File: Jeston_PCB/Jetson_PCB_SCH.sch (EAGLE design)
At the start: 4 parts, among them Q2 NTD3055L104G

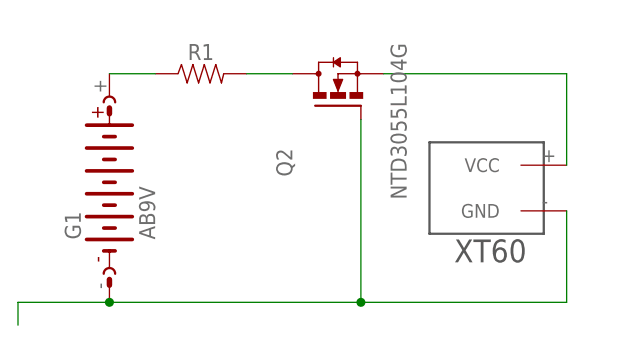
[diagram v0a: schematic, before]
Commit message: replaced battery port with XT60
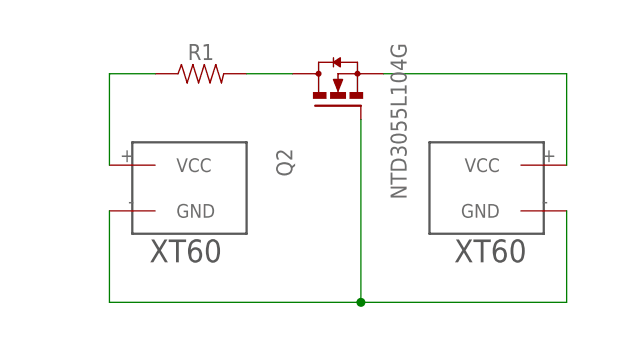
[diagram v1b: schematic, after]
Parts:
- removed G1: AB9V, battery:AB9V
- added U$2: XT60, XT60:XT60
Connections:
- net N$1: now also U$2.GND; no longer G1.-
- net N$2: now also U$2.VCC; no longer G1.+
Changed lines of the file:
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@@
 </classes>
 <parts>
-<part name="G1" library="battery" library_urn="urn:adsk.eagle:library:109" deviceset="AB9V" device="" package3d_urn="urn:adsk.eagle:package:4600/1"/>
 <part name="R1" library="SparkFun-Resistors" deviceset="RESISTOR" device="AXIAL-0.3-KIT" value=" "/>
 <part name="Q2" library="Transistor" library_urn="urn:adsk.eagle:library:11396518" deviceset="NTD3055L104G" device="" package3d_urn="urn:adsk.eagle:package:10893256/2"/>
 <part name="U$1" library="XT60" deviceset="XT60" device=""/>
+<part name="U$2" library="XT60" deviceset="XT60" device=""/>
 </parts>
 <sheets>
@@
 </plain>
 <instances>
-<instance part="G1" gate="G$1" x="10.16" y="73.66" smashed="yes" rot="R90">
-<attribute name="NAME" x="6.985" y="67.945" size="1.778" layer="95" rot="R90"/>
-<attribute name="VALUE" x="15.24" y="67.945" size="1.778" layer="96" rot="R90"/>
-</instance>
 <instance part="R1" gate="G$1" x="20.32" y="86.36" smashed="yes">
 <attribute name="NAME" x="20.32" y="87.884" size="1.778" layer="95" font="vector" align="bottom-center"/>
@@
 </instance>
 <instance part="U$1" gate="G$1" x="55.88" y="73.66" smashed="yes" rot="R180"/>
+<instance part="U$2" gate="G$1" x="15.24" y="73.66" smashed="yes" rot="MR180"/>
 </instances>
 <busses>
@@
 <net name="N$1" class="0">
 <segment>
-<pinref part="G1" gate="G$1" pin="-"/>
-<wire x1="0" y1="58.42" x2="0" y2="60.96" width="0.1524" layer="91"/>
-<wire x1="0" y1="60.96" x2="10.16" y2="60.96" width="0.1524" layer="91"/>
 <wire x1="10.16" y1="60.96" x2="38.1" y2="60.96" width="0.1524" layer="91"/>
-<junction x="10.16" y="60.96"/>
 <wire x1="38.1" y1="60.96" x2="60.96" y2="60.96" width="0.1524" layer="91"/>
 <wire x1="60.96" y1="71.12" x2="60.96" y2="60.96" width="0.1524" layer="91"/>
@@
 <pinref part="Q2" gate="G$1" pin="G"/>
 <pinref part="U$1" gate="G$1" pin="GND"/>
+<pinref part="U$2" gate="G$1" pin="GND"/>
+<wire x1="10.16" y1="71.12" x2="10.16" y2="60.96" width="0.1524" layer="91"/>
 </segment>
 </net>
 <net name="N$2" class="0">
 <segment>
-<pinref part="G1" gate="G$1" pin="+"/>
 <wire x1="10.16" y1="86.36" x2="15.24" y2="86.36" width="0.1524" layer="91"/>
 <pinref part="R1" gate="G$1" pin="1"/>
+<pinref part="U$2" gate="G$1" pin="VCC"/>
+<wire x1="10.16" y1="86.36" x2="10.16" y2="76.2" width="0.1524" layer="91"/>
 </segment>
 </net>

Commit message: replacing ports to pins, different resistor footprint
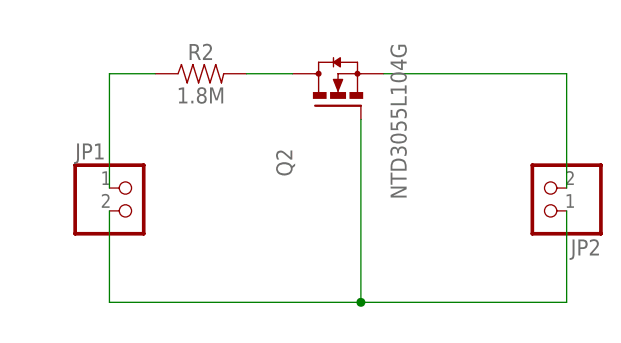
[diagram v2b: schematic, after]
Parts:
- removed R1: (no value), SparkFun-Resistors:RESISTORAXIAL-0.3-KIT
- removed U$1, U$2: XT60, XT60:XT60
- added JP1, JP2: (no value), pinhead:PINHD-1X2
- added R2: 1.8M, SparkFun-Resistors:1.8MOHM
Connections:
- net N$1: now also JP1.2, JP2.1; no longer U$1.GND, U$2.GND
- net N$2: now also JP1.1, R2.1; no longer R1.1, U$2.VCC
- net N$3: now also R2.2; no longer R1.2
- net N$4: now also JP2.2; no longer U$1.VCC
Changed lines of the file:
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@@
 </classes>
 <parts>
-<part name="R1" library="SparkFun-Resistors" deviceset="RESISTOR" device="AXIAL-0.3-KIT" value=" "/>
 <part name="Q2" library="Transistor" library_urn="urn:adsk.eagle:library:11396518" deviceset="NTD3055L104G" device="" package3d_urn="urn:adsk.eagle:package:10893256/2"/>
-<part name="U$1" library="XT60" deviceset="XT60" device=""/>
-<part name="U$2" library="XT60" deviceset="XT60" device=""/>
+<part name="JP1" library="pinhead" library_urn="urn:adsk.eagle:library:325" deviceset="PINHD-1X2" device="" package3d_urn="urn:adsk.eagle:package:22435/2"/>
+<part name="JP2" library="pinhead" library_urn="urn:adsk.eagle:library:325" deviceset="PINHD-1X2" device="" package3d_urn="urn:adsk.eagle:package:22435/2"/>
+<part name="R2" library="SparkFun-Resistors" deviceset="1.8MOHM" device="" value="1.8M"/>
 </parts>
 <sheets>
@@
 </plain>
 <instances>
-<instance part="R1" gate="G$1" x="20.32" y="86.36" smashed="yes">
-<attribute name="NAME" x="20.32" y="87.884" size="1.778" layer="95" font="vector" align="bottom-center"/>
-<attribute name="VALUE" x="20.32" y="84.836" size="1.778" layer="96" font="vector" align="top-center"/>
-</instance>
 <instance part="Q2" gate="G$1" x="35.56" y="83.82" smashed="yes" rot="R90">
 <attribute name="NAME" x="30.48" y="74.93" size="1.778" layer="95" rot="R90"/>
 <attribute name="VALUE" x="43.18" y="72.39" size="1.778" layer="96" rot="R90"/>
 </instance>
-<instance part="U$1" gate="G$1" x="55.88" y="73.66" smashed="yes" rot="R180"/>
-<instance part="U$2" gate="G$1" x="15.24" y="73.66" smashed="yes" rot="MR180"/>
+<instance part="JP1" gate="G$1" x="12.7" y="71.12" smashed="yes">
+<attribute name="NAME" x="6.35" y="76.835" size="1.778" layer="95"/>
+<attribute name="VALUE" x="6.35" y="66.04" size="1.778" layer="96"/>
+</instance>
+<instance part="JP2" gate="G$1" x="58.42" y="73.66" smashed="yes" rot="R180">
+<attribute name="NAME" x="64.77" y="67.945" size="1.778" layer="95" rot="R180"/>
+<attribute name="VALUE" x="64.77" y="78.74" size="1.778" layer="96" rot="R180"/>
+</instance>
+<instance part="R2" gate="G$1" x="20.32" y="86.36" smashed="yes">
+<attribute name="NAME" x="20.32" y="87.884" size="1.778" layer="95" font="vector" align="bottom-center"/>
+<attribute name="VALUE" x="20.32" y="84.836" size="1.778" layer="96" font="vector" align="top-center"/>
+</instance>
 </instances>
 <busses>
@@
 <junction x="38.1" y="60.96"/>
 <pinref part="Q2" gate="G$1" pin="G"/>
-<pinref part="U$1" gate="G$1" pin="GND"/>
-<pinref part="U$2" gate="G$1" pin="GND"/>
 <wire x1="10.16" y1="71.12" x2="10.16" y2="60.96" width="0.1524" layer="91"/>
+<pinref part="JP2" gate="G$1" pin="1"/>
+<pinref part="JP1" gate="G$1" pin="2"/>
 </segment>
 </net>
@@
 <segment>
 <wire x1="10.16" y1="86.36" x2="15.24" y2="86.36" width="0.1524" layer="91"/>
-<pinref part="R1" gate="G$1" pin="1"/>
-<pinref part="U$2" gate="G$1" pin="VCC"/>
-<wire x1="10.16" y1="86.36" x2="10.16" y2="76.2" width="0.1524" layer="91"/>
+<wire x1="10.16" y1="86.36" x2="10.16" y2="73.66" width="0.1524" layer="91"/>
+<pinref part="JP1" gate="G$1" pin="1"/>
+<pinref part="R2" gate="G$1" pin="1"/>
 </segment>
 </net>
 <net name="N$3" class="0">
 <segment>
-<pinref part="R1" gate="G$1" pin="2"/>
 <wire x1="25.4" y1="86.36" x2="30.48" y2="86.36" width="0.1524" layer="91"/>
 <pinref part="Q2" gate="G$1" pin="D"/>
+<pinref part="R2" gate="G$1" pin="2"/>
 </segment>
 </net>
@@
 <segment>
 <wire x1="40.64" y1="86.36" x2="60.96" y2="86.36" width="0.1524" layer="91"/>
-<wire x1="60.96" y1="86.36" x2="60.96" y2="76.2" width="0.1524" layer="91"/>
+<wire x1="60.96" y1="86.36" x2="60.96" y2="73.66" width="0.1524" layer="91"/>
 <pinref part="Q2" gate="G$1" pin="S"/>
-<pinref part="U$1" gate="G$1" pin="VCC"/>
+<pinref part="JP2" gate="G$1" pin="2"/>
 </segment>
 </net>
